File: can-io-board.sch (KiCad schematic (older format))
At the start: 21 parts, among them P1 CONN_01X08, P2 CONN_01X08, U1 STM32F302K8U6, U2 MCP1703, U3 MAX3051, X1 XTAL-SMD-4-PADS

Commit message: routing done
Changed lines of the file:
@@
 $EndDescr
-$Comp
-L STM32F302K8U6 U1
-U 1 1 56D60A29
-P 4600 4450
-F 0 "U1" H 5000 6000 60  0000 C CNN
-F 1 "STM32F302K8U6" H 4500 6000 60  0000 C CNN
-F 2 "Housings_DFN_QFN:QFN-32-1EP_5x5mm_Pitch0.5mm" H 4600 3950 60  0001 C CNN
-F 3 "DOCUMENTATION" H 4600 3950 60  0001 C CNN
-	1    4600 4450
-	1    0    0    -1
-$EndComp
 $Comp
 L XTAL-SMD-4-PADS X1
@@
 Text Label 1450 4350 0    60   ~ 0
 LED
-Text Label 5450 4600 0    60   ~ 0
+Text Label 5450 3500 0    60   ~ 0
 LED
 $Comp
@@
 Text Notes 6700 5100 0    60   ~ 0
 JTRST
-Text Label 7700 2100 0    60   ~ 0
+Text Label 7700 2300 0    60   ~ 0
 IO_PB5_SPI3MOSI
 Text Label 7700 2200 0    60   ~ 0
 IO_PB4_SPI3MISO_UART2RX
-Text Label 7700 2300 0    60   ~ 0
+Text Label 7700 2100 0    60   ~ 0
 IO_PB3_SPI3SCK_UART2TX
 Text Label 5100 1900 0    60   ~ 0
@@
 Text Label 7700 2000 0    60   ~ 0
 IO_PA10_I2C2SDA_UART1RX
-NoConn ~ 5350 3500
 NoConn ~ 5350 3600
 NoConn ~ 5350 3900
@@
 	4900 1550 4900 1600
 Wire Wire Line
-	5450 4600 5350 4600
-Wire Wire Line
 	5450 5400 5350 5400
 Wire Wire Line
@@
 Text Label 5100 2200 0    60   ~ 0
 IO_PA8_TIM16CH1_ADC10
+$Comp
+L STM32F302K8U6 U1
+U 1 1 56D60A29
+P 4600 4450
+F 0 "U1" H 5000 6000 60  0000 C CNN
+F 1 "STM32F302K8U6" H 4500 6000 60  0000 C CNN
+F 2 "Housings_DFN_QFN:QFN-32-1EP_5x5mm_Pitch0.5mm" H 4600 3950 60  0001 C CNN
+F 3 "DOCUMENTATION" H 4600 3950 60  0001 C CNN
+	1    4600 4450
+	1    0    0    -1
+$EndComp
+NoConn ~ 5350 4600
+Wire Wire Line
+	5450 3500 5350 3500
 $EndSCHEMATC

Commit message: fix pin name, add silkscreen
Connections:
- net labels added: IO_PA6_TIM16CH1_ADC10
- net labels removed: IO_PA8_TIM16CH1_ADC10
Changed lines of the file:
@@
 IO_PA7_TIM17CH1_ADC15
 Text Label 5450 3700 0    60   ~ 0
-IO_PA8_TIM16CH1_ADC10
+IO_PA6_TIM16CH1_ADC10
 Wire Wire Line
 	5350 3400 5450 3400
@@
 IO_PA7_TIM17CH1_ADC15
 Text Label 5100 2200 0    60   ~ 0
-IO_PA8_TIM16CH1_ADC10
+IO_PA6_TIM16CH1_ADC10
 $Comp
 L STM32F302K8U6 U1

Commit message: oscillator reference
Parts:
- X1: value XTAL-SMD-4-PADS -> 16MHz 10ppm; Digikey (none) -> CTX847CT-ND
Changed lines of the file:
@@
 U 1 1 56D60A5D
 P 5950 5850
-F 0 "X1" H 5950 6050 60  0000 C CNN
-F 1 "XTAL-SMD-4-PADS" H 5950 6150 60  0000 C CNN
+F 0 "X1" H 5950 5950 60  0000 C CNN
+F 1 "16MHz 10ppm" H 5950 6050 60  0000 C CNN
 F 2 "_div:_TSX-3225-SMD-XTAL" H 5950 5850 60  0001 C CNN
 F 3 "" H 5950 5850 60  0000 C CNN
+F 4 "CTX847CT-ND" H 5950 6150 60  0000 C CNN "Digikey"
 	1    5950 5850
 	1    0    0    -1

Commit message: Start layout on RevB
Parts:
- removed P1, P2: CONN_01X08, _connectors:_Pin2mm_8, symbol CONN_01X08
- added H1, H2: MountingHole M2, MountingHole:MountingHole_2.2mm_M2_DIN965, symbol Mechanical:MountingHole
- added J1: Conn_02x13_Odd_Even, Connector_PinHeader_2.00mm:PinHeader_2x13_P2.00mm_Vertical, symbol Connector_Generic:Conn_02x13_Odd_Even
- C1, C10, C2, C3, C4, C5, C6, C7, C8, C9: symbol C -> can-io-board-rescue:C-device
- CONN1: symbol SWD/DEBUG -> can-io-board-rescue:SWD_DEBUG
- CONN2, CONN3: symbol CAN -> _connectors:CAN
- D1: symbol LED -> can-io-board-rescue:LED
- R1: symbol R -> can-io-board-rescue:R-device
- U1: symbol STM32F302K8U6 -> _stm32:STM32F302K8U6
- U2: symbol MCP1703 -> _linear-regulators:MCP1703
- U3: footprint _std:_SOT23-8 -> Package_SO:SOIC-8_3.9x4.9mm_P1.27mm; symbol MAX3051 -> _div:MAX3051
- X1: symbol XTAL-SMD-4-PADS -> _div:XTAL-SMD-4-PADS
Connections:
- net labels removed: CAN_EN
- wire segments 104 -> 130
- no-connect marks 3 -> 4

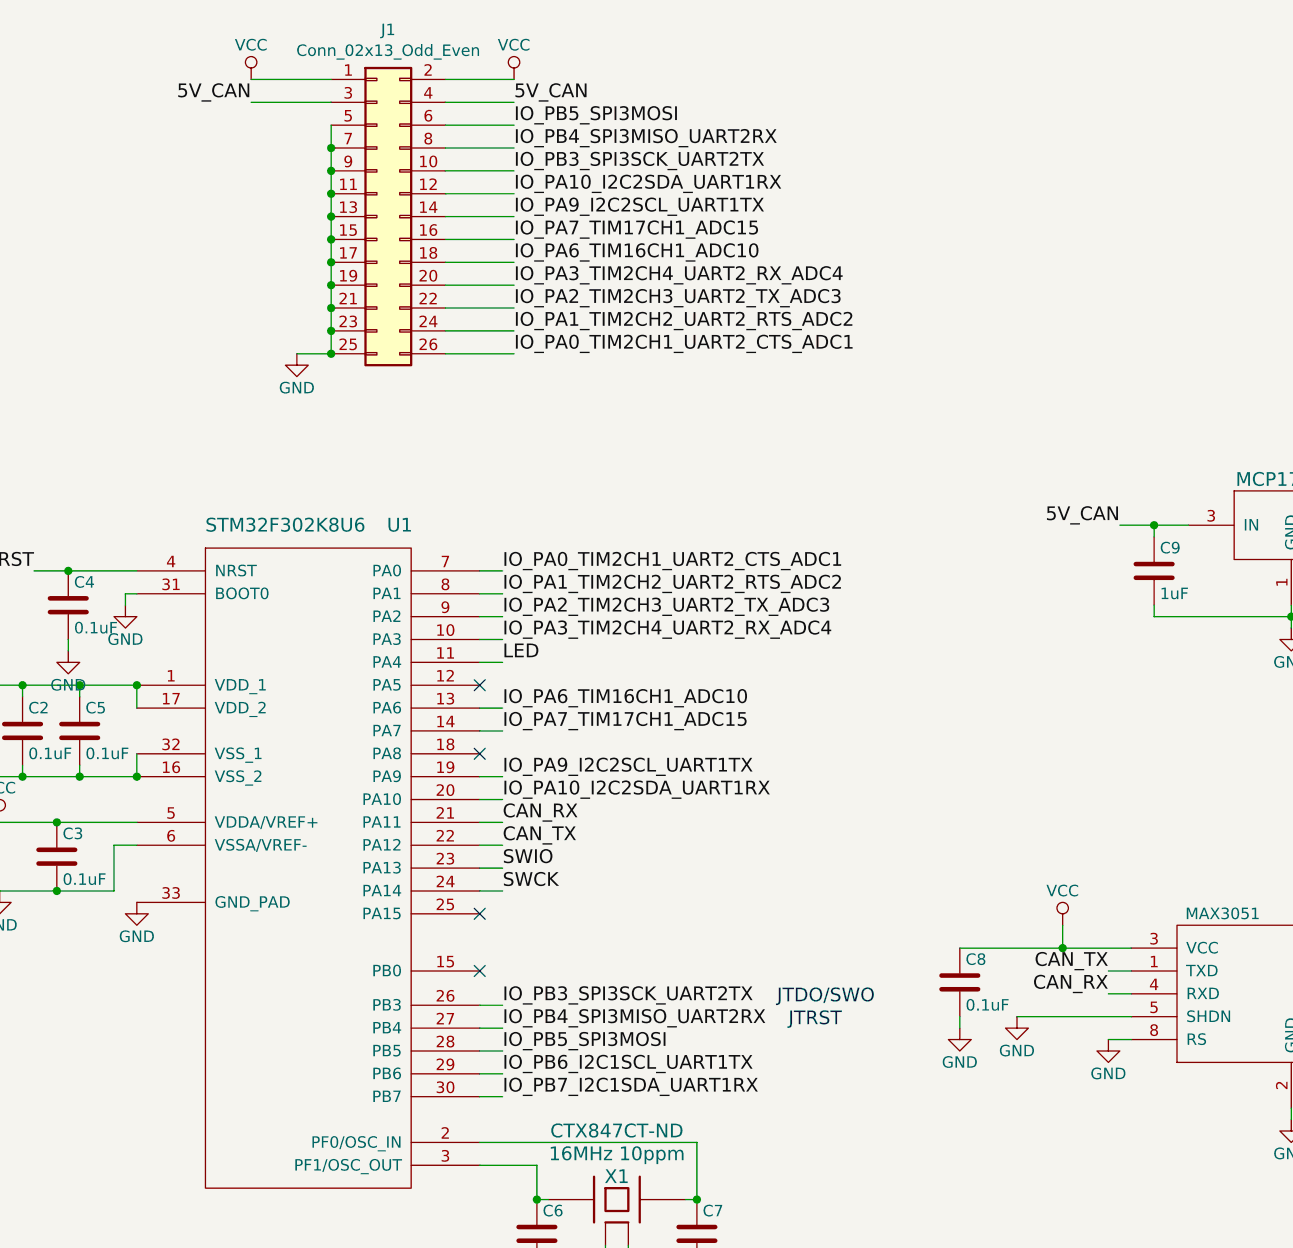
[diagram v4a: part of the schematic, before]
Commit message: Reduced number of IO, use PicoBlade connector
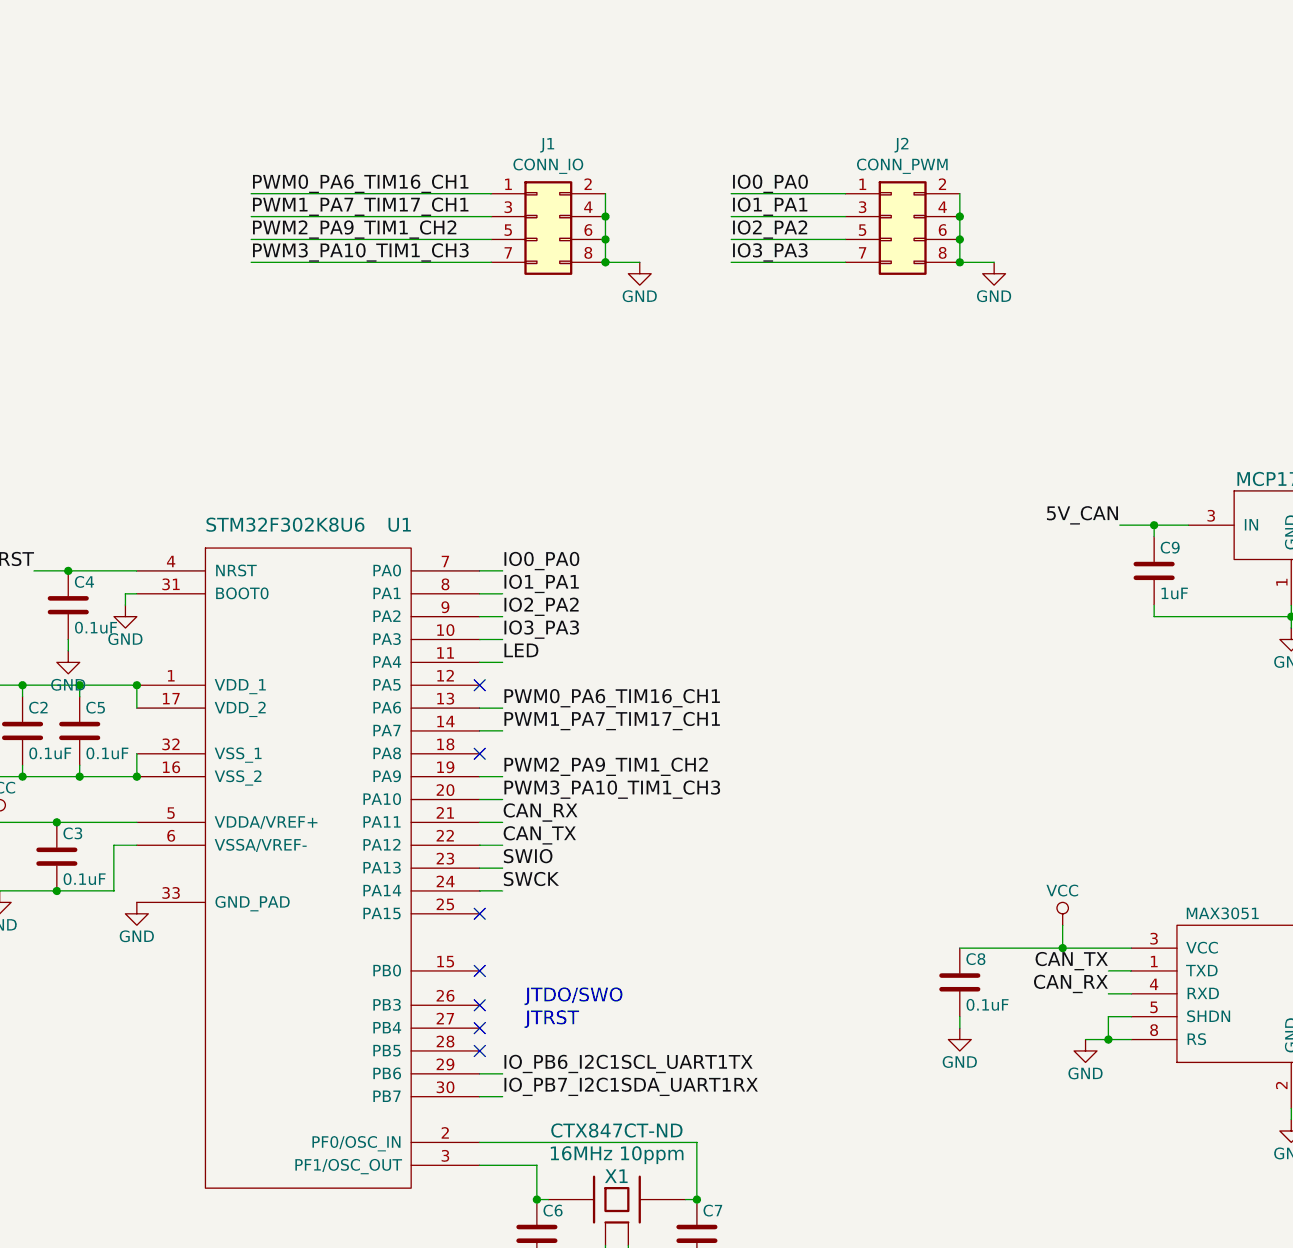
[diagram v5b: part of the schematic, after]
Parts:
- removed J1: Conn_02x13_Odd_Even, Connector_PinHeader_2.00mm:PinHeader_2x13_P2.00mm_Vertical, symbol Connector_Generic:Conn_02x13_Odd_Even
- added J1: CONN_IO, Connector_Molex:Molex_PicoBlade_53261-0871_1x08-1MP_P1.25mm_Horizontal, symbol Connector_Generic:Conn_02x04_Odd_Even
- added J2: CONN_PWM, Connector_Molex:Molex_PicoBlade_53261-0871_1x08-1MP_P1.25mm_Horizontal, symbol Connector_Generic:Conn_02x04_Odd_Even
- C1, C10, C9: footprint Capacitors_SMD:C_0603 -> Capacitor_SMD:C_0603_1608Metric
- C2, C3, C4, C5, C6, C7, C8: footprint Capacitors_SMD:C_0603 -> Capacitor_SMD:C_0402_1005Metric
- CONN1: footprint Connectors_Molex:Connector_Molex_PicoBlade_53047-0710 -> _connectors:_Solder_Pad1.27_7
- CONN2, CONN3: footprint Connectors_Molex:Connector_Molex_PicoBlade_53261-0471 -> Connector_Molex:Molex_PicoBlade_53261-0471_1x04-1MP_P1.25mm_Horizontal
- R1: footprint Resistors_SMD:R_0603 -> Resistor_SMD:R_0402_1005Metric
- U3: footprint Package_SO:SOIC-8_3.9x4.9mm_P1.27mm -> _std:_SOT23-8
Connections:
- net GND: now also J1.2 (Pin_2), J1.4 (Pin_4), J1.6 (Pin_6), J1.8 (Pin_8), J2.2 (Pin_2), J2.4 (Pin_4), J2.6 (Pin_6), J2.8 (Pin_8)
- net IO_PA0_TIM2CH1_UART2_CTS_ADC1 renamed IO0_PA0
- net IO0_PA0: now also J2.1 (Pin_1)
- net IO_PA10_I2C2SDA_UART1RX renamed PWM3_PA10_TIM1_CH3
- net PWM3_PA10_TIM1_CH3: now also J1.7 (Pin_7)
- net IO_PA1_TIM2CH2_UART2_RTS_ADC2 renamed IO1_PA1
- net IO1_PA1: now also J2.3 (Pin_3)
- net IO_PA2_TIM2CH3_UART2_TX_ADC3 renamed IO2_PA2
- net IO2_PA2: now also J2.5 (Pin_5)
- net IO_PA3_TIM2CH4_UART2_RX_ADC4 renamed IO3_PA3
- net IO3_PA3: now also J2.7 (Pin_7)
- net IO_PA6_TIM16CH1_ADC10 renamed PWM0_PA6_TIM16_CH1
- net PWM0_PA6_TIM16_CH1: now also J1.1 (Pin_1)
- net IO_PA7_TIM17CH1_ADC15 renamed PWM1_PA7_TIM17_CH1
- net PWM1_PA7_TIM17_CH1: now also J1.3 (Pin_3)
- net IO_PA9_I2C2SCL_UART1TX renamed PWM2_PA9_TIM1_CH2
- net PWM2_PA9_TIM1_CH2: now also J1.5 (Pin_5)
- net IO_PB3_SPI3SCK_UART2TX: no longer names the net of U1.26 (PB3)
- net IO_PB4_SPI3MISO_UART2RX: no longer names the net of U1.27 (PB4)
- net IO_PB5_SPI3MOSI: no longer names the net of U1.28 (PB5)
- no-connect marks 4 -> 7

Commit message: Routing almost finished
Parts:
- removed H1, H2: MountingHole M2, MountingHole:MountingHole_2.2mm_M2_DIN965, symbol Mechanical:MountingHole
- D1: footprint LEDs:LED-0603 -> LED_SMD:LED_0603_1608Metric
- X1: footprint _div:_TSX-3225-SMD-XTAL -> Crystal:Crystal_SMD_SeikoEpson_TSX3225-4Pin_3.2x2.5mm
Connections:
- net GND: now also D1.1 (K); no longer R1.2
- net LED: now also R1.1; no longer D1.2 (A)
- new net: D1.2 (A), R1.2
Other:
- moved on the sheet: D1, R1
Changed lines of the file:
@@
 F 0 "X1" H 5950 5950 60  0000 C CNN
 F 1 "16MHz 10ppm" H 5950 6050 60  0000 C CNN
-F 2 "_div:_TSX-3225-SMD-XTAL" H 5950 5850 60  0001 C CNN
+F 2 "Crystal:Crystal_SMD_SeikoEpson_TSX3225-4Pin_3.2x2.5mm" H 5950 5850 60  0001 C CNN
 F 3 "" H 5950 5850 60  0000 C CNN
 F 4 "CTX847CT-ND" H 5950 6150 60  0000 C CNN "Digikey"
@@
 L can-io-board-rescue:LED D1
 U 1 1 56D63FB2
-P 1450 4600
-F 0 "D1" H 1450 4700 50  0000 C CNN
-F 1 "LED" H 1450 4500 50  0000 C CNN
-F 2 "LEDs:LED-0603" H 1450 4600 50  0001 C CNN
-F 3 "" H 1450 4600 50  0000 C CNN
-	1    1450 4600
+P 1450 4950
+F 0 "D1" H 1450 5050 50  0000 C CNN
+F 1 "LED" H 1450 4850 50  0000 C CNN
+F 2 "LED_SMD:LED_0603_1608Metric" H 1450 4950 50  0001 C CNN
+F 3 "" H 1450 4950 50  0000 C CNN
+	1    1450 4950
 	0    -1   -1   0
 $EndComp
@@
 L can-io-board-rescue:R-device R1
 U 1 1 56D64054
-P 1450 5000
-F 0 "R1" V 1530 5000 50  0000 C CNN
-F 1 "510" V 1450 5000 50  0000 C CNN
-F 2 "Resistor_SMD:R_0402_1005Metric" V 1380 5000 50  0001 C CNN
-F 3 "" H 1450 5000 50  0000 C CNN
-	1    1450 5000
+P 1450 4550
+F 0 "R1" V 1530 4550 50  0000 C CNN
+F 1 "510" V 1450 4550 50  0000 C CNN
+F 2 "Resistor_SMD:R_0402_1005Metric" V 1380 4550 50  0001 C CNN
+F 3 "" H 1450 4550 50  0000 C CNN
+	1    1450 4550
 	1    0    0    -1
 $EndComp
@@
 	1450 4350 1450 4400
 Wire Wire Line
-	1450 4800 1450 4850
+	1450 4700 1450 4750
 Wire Wire Line
 	1450 5200 1450 5150
@@
 	1    0    0    -1
 $EndComp
-$Comp
-L Mechanical:MountingHole H1
-U 1 1 5BC6A1CF
-P 1350 7050
-F 0 "H1" H 1450 7096 50  0000 L CNN
-F 1 "MountingHole M2" H 1450 7005 50  0000 L CNN
-F 2 "MountingHole:MountingHole_2.2mm_M2_DIN965" H 1350 7050 50  0001 C CNN
-F 3 "~" H 1350 7050 50  0001 C CNN
-	1    1350 7050
-	1    0    0    -1
-$EndComp
-$Comp
-L Mechanical:MountingHole H2
-U 1 1 5BC6A228
-P 1350 7250
-F 0 "H2" H 1450 7296 50  0000 L CNN
-F 1 "MountingHole M2" H 1450 7205 50  0000 L CNN
-F 2 "MountingHole:MountingHole_2.2mm_M2_DIN965" H 1350 7250 50  0001 C CNN
-F 3 "~" H 1350 7250 50  0001 C CNN
-	1    1350 7250
-	1    0    0    -1
-$EndComp

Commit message: Silkscreen placement
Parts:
- CONN1: footprint _connectors:_Solder_Pad1.27_7 -> Connector_Molex:Molex_PicoBlade_53048-1410_1x07_P1.25mm_Horizontal
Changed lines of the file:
@@
 F 0 "CONN1" H 1400 2250 50  0000 C CNN
 F 1 "SWD/DEBUG" H 1400 1350 50  0000 C CNN
-F 2 "_connectors:_Solder_Pad1.27_7" H 1400 1750 50  0001 C CNN
+F 2 "Connector_Molex:Molex_PicoBlade_53048-1410_1x07_P1.25mm_Horizontal" H 1400 1750 50  0001 C CNN
 F 3 "DOCUMENTATION" H 1400 1750 50  0001 C CNN
 	1    1400 1800

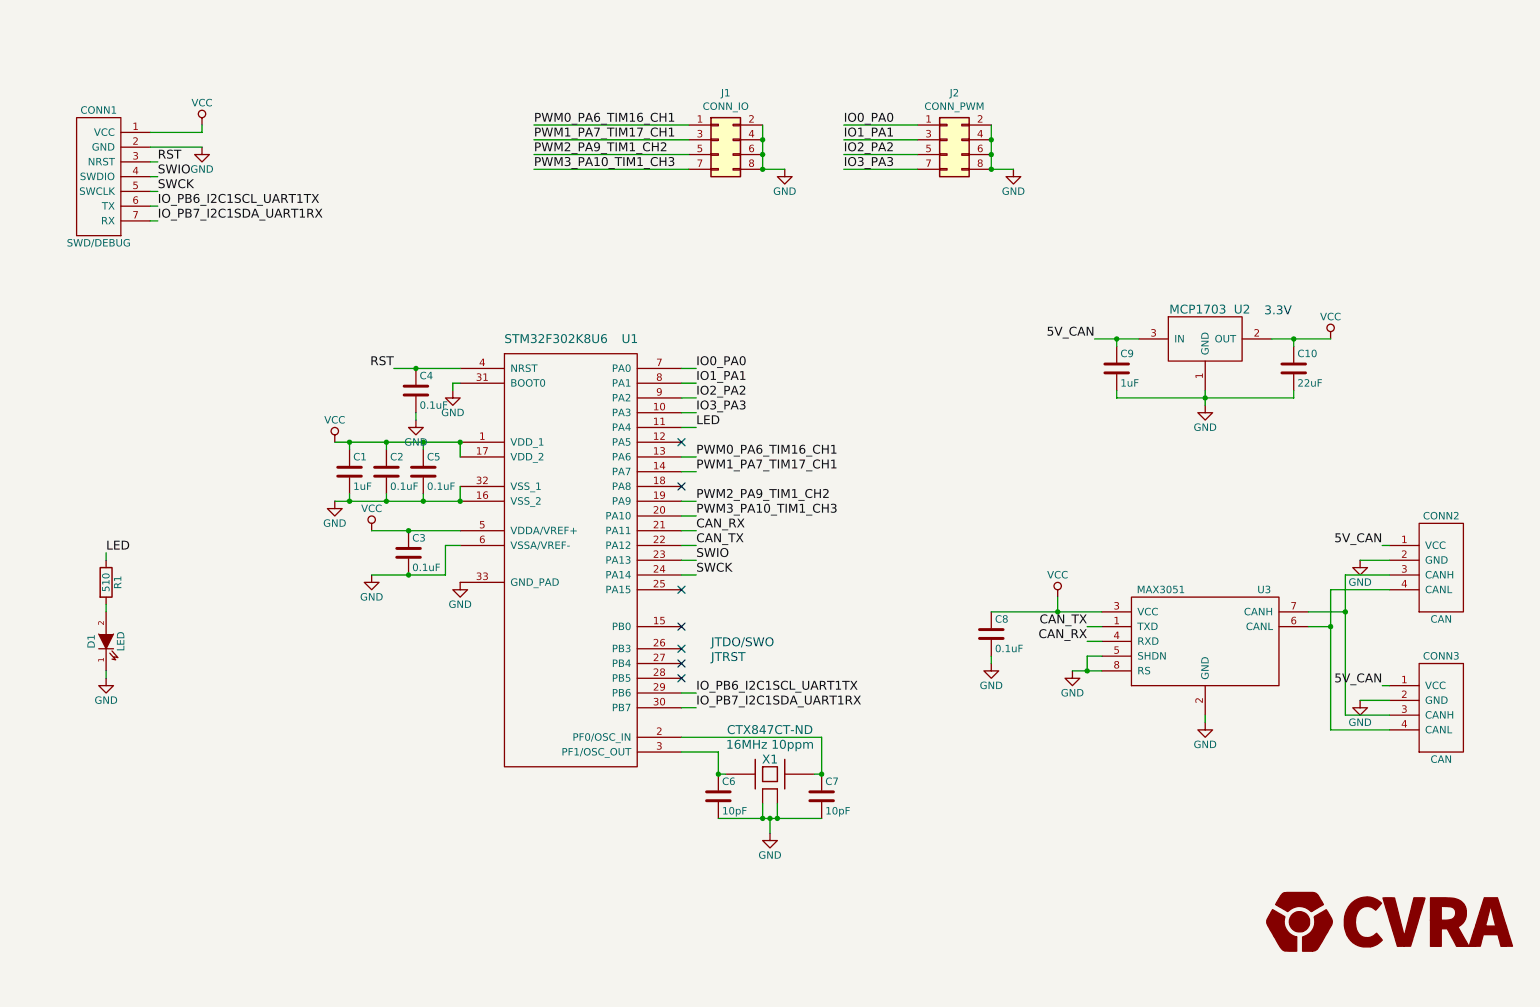
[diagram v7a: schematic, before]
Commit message: Add Digikey ref in schematic, add BOM
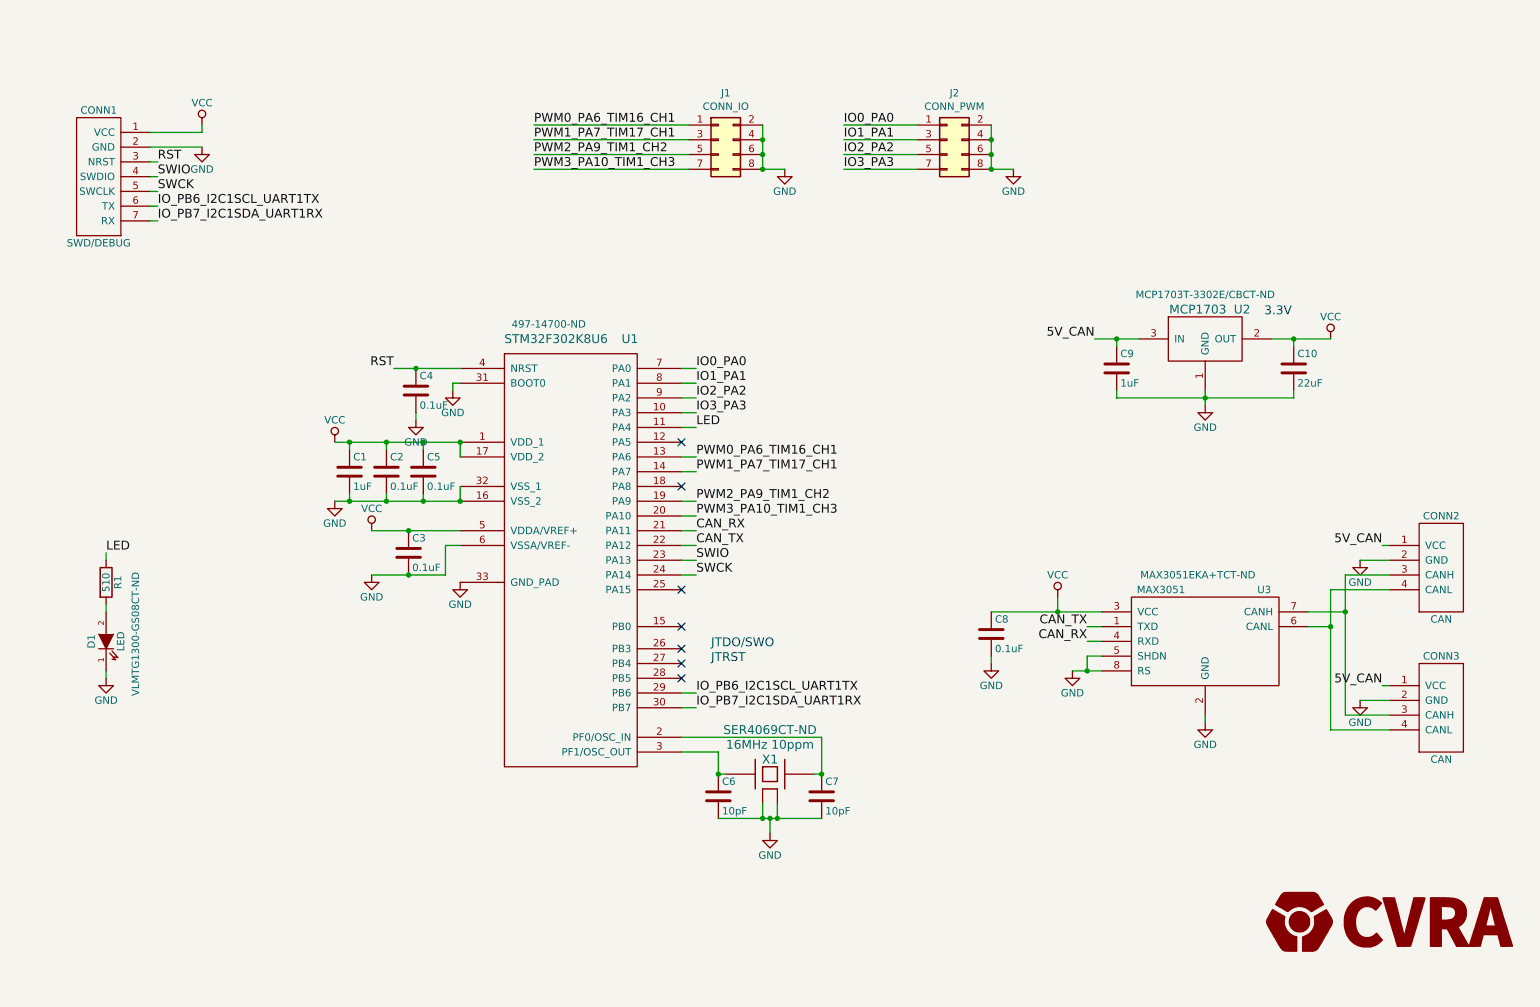
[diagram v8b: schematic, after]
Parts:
- D1: Digikey (none) -> VLMTG1300-GS08CT-ND
- U1: Digikey (none) -> 497-14700-ND
- U2: Digikey (none) -> MCP1703T-3302E/CBCT-ND
- U3: Digikey (none) -> MAX3051EKA+TCT-ND
- X1: Digikey CTX847CT-ND -> SER4069CT-ND
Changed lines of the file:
@@
 F 2 "Crystal:Crystal_SMD_SeikoEpson_TSX3225-4Pin_3.2x2.5mm" H 5950 5850 60  0001 C CNN
 F 3 "" H 5950 5850 60  0000 C CNN
-F 4 "CTX847CT-ND" H 5950 6150 60  0000 C CNN "Digikey"
+F 4 "SER4069CT-ND" H 5950 6150 60  0000 C CNN "Digikey"
 	1    5950 5850
 	1    0    0    -1
@@
 F 2 "_std:_SOT23-8" H 8900 4950 50  0001 C CNN
 F 3 "CAN Transceiver" H 8900 4950 50  0001 C CNN
+F 4 "MAX3051EKA+TCT-ND" H 8850 5400 50  0000 C CNN "Digikey"
 	1    8900 4950
 	1    0    0    -1
@@
 F 2 "_div:_MCP1703-SOT-23A" H 8800 3350 60  0001 C CNN
 F 3 "" H 8800 3350 60  0000 C CNN
+F 4 "MCP1703T-3302E/CBCT-ND" H 8900 3200 50  0000 C CNN "Digikey"
 	1    8900 2900
 	1    0    0    -1
@@
 F 2 "LED_SMD:LED_0603_1608Metric" H 1450 4950 50  0001 C CNN
 F 3 "" H 1450 4950 50  0000 C CNN
+F 4 "VLMTG1300-GS08CT-ND" H 1500 4750 50  0000 C CNN "Digikey"
 	1    1450 4950
 	0    -1   -1   0
@@
 F 2 "Housings_DFN_QFN:QFN-32-1EP_5x5mm_Pitch0.5mm" H 4600 3950 60  0001 C CNN
 F 3 "DOCUMENTATION" H 4600 3950 60  0001 C CNN
+F 4 "497-14700-ND" H 4450 6100 50  0000 C CNN "Digikey"
 	1    4600 4450
 	1    0    0    -1
